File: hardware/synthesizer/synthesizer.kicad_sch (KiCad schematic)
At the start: 18 parts, among them J1 USB_C_Receptacle_PowerOnly_6P, J2 Conn_Coaxial, J3 Conn_Coaxial, U1 STM32H723VGTx

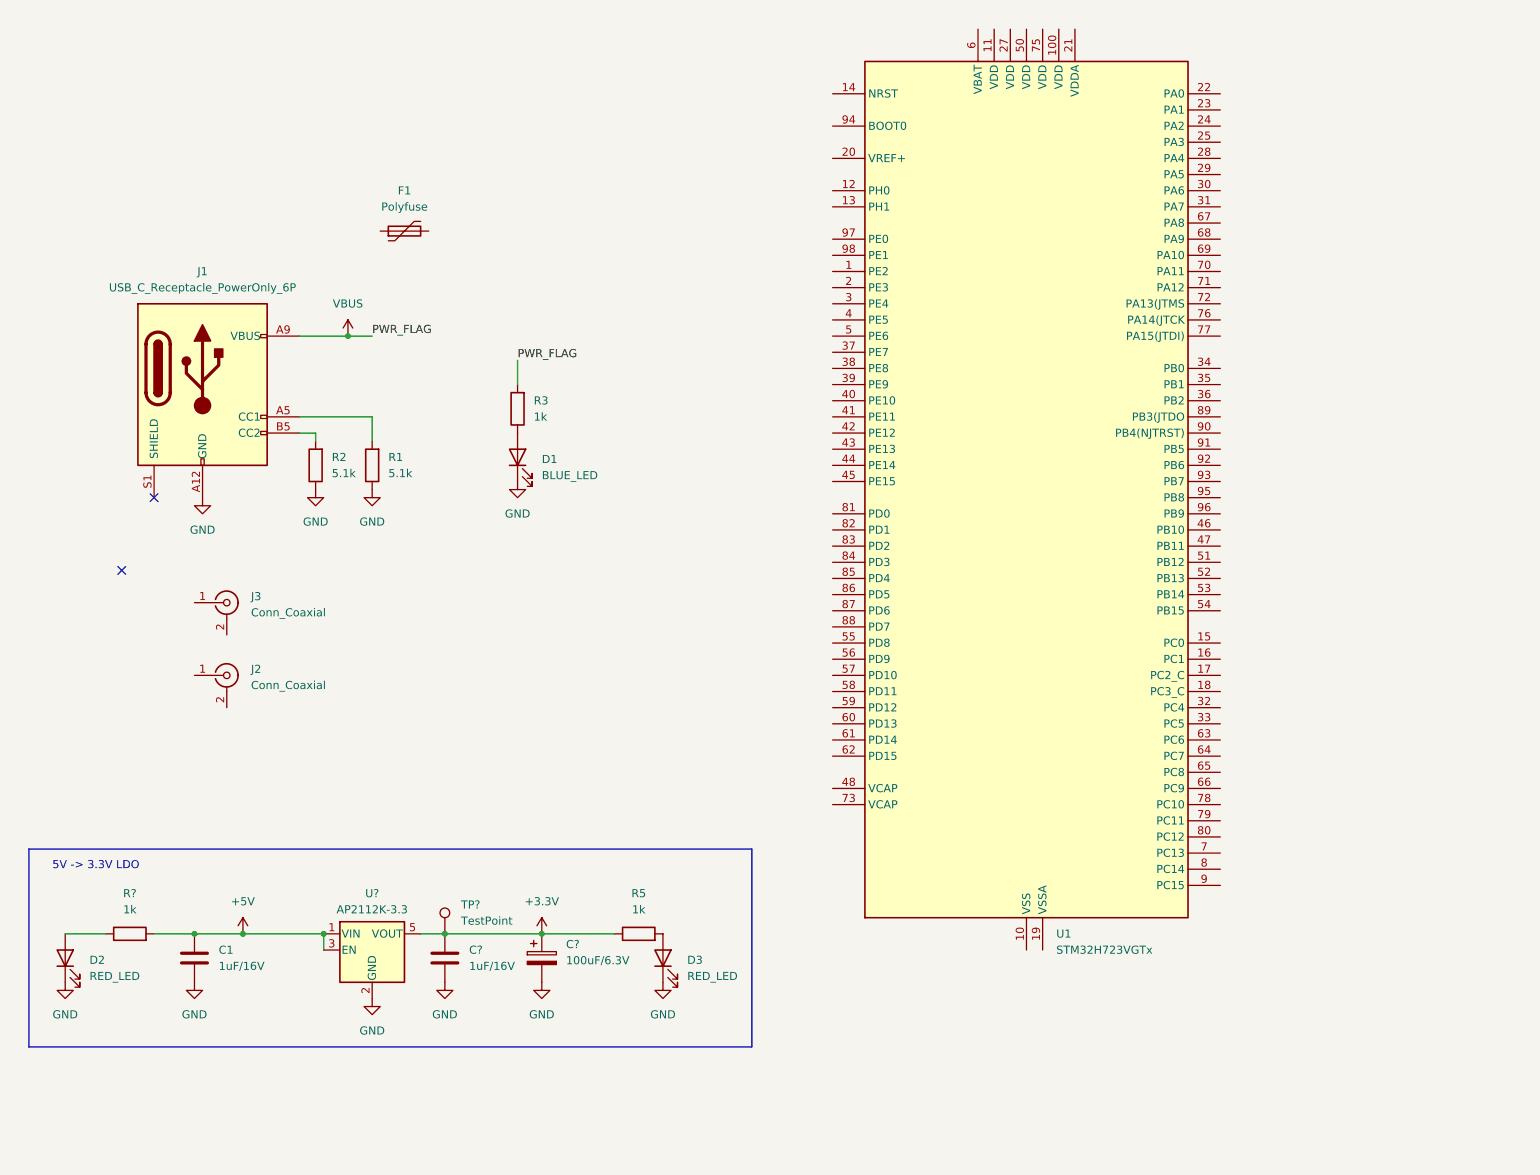
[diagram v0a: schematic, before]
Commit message: add jtag connector + continue cw8 report
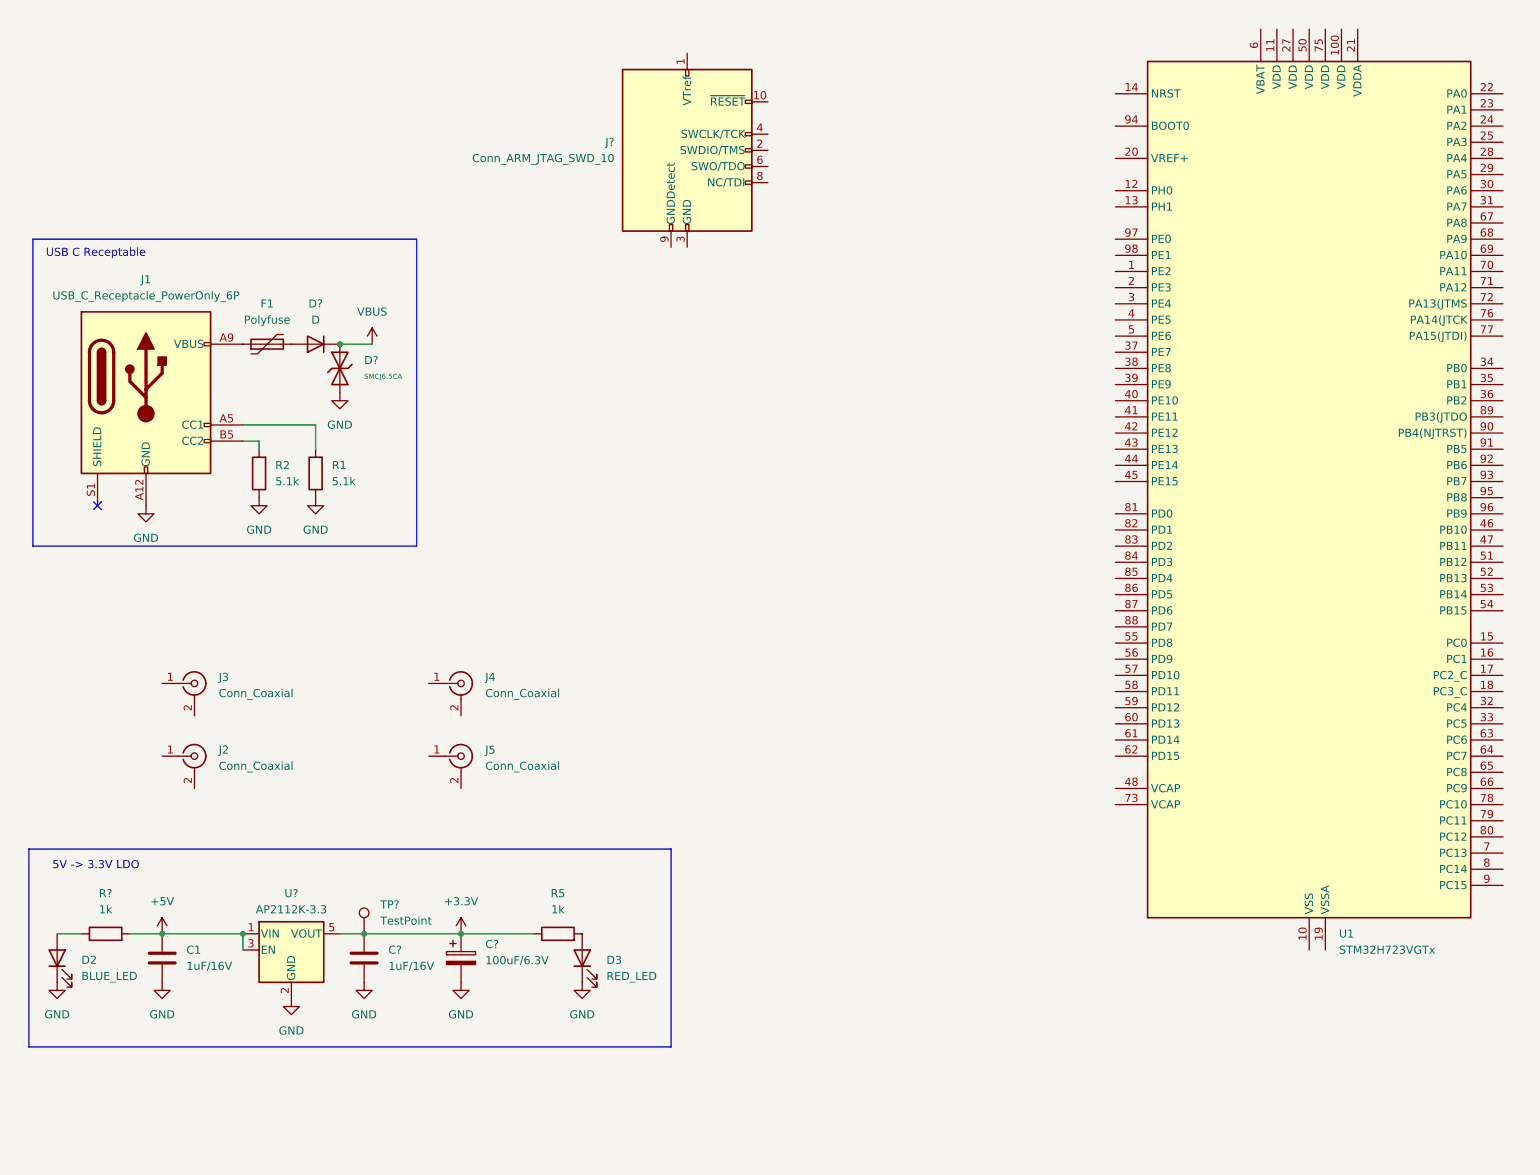
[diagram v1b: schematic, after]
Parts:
- removed D1: BLUE_LED, symbol Device:LED
- removed R3: 1k, symbol Device:R
- added D?: D, symbol Device:D
- added D?: SMCJ6.5CA, PCM_JLCPCB:D_SMC, symbol PCM_JLCPCB-Diodes:TVS-Bi,SMCJ6.5CA,(3)
- added J4, J5: Conn_Coaxial, Connector_Coaxial:SMA_BAT_Wireless_BWSMA-KWE-Z001, symbol Connector:Conn_Coaxial
- added J?: Conn_ARM_JTAG_SWD_10, Connector_PinHeader_1.27mm:PinHeader_2x05_P1.27mm_Vertical, symbol Connector:Conn_ARM_JTAG_SWD_10
- D2: value RED_LED -> BLUE_LED
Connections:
- net GND: now also D?.1
- net VBUS: now also D?.1 (K), D?.2; no longer J1.A9 (VBUS), J1.B9 (VBUS)
- net at F1.1: now also J1.A9 (VBUS), J1.B9 (VBUS)
- net at F1.2: now also D?.2 (A)
- new net: J?.3 (GND), J?.5 (GND)
- no-connect marks 2 -> 1
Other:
- note added: "USB C Receptable"
- moved on the sheet: C1, C?, D2, D3, F1, J1, J2, J3, R1, R2, R5, R?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

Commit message: add ethernet to synthesizer
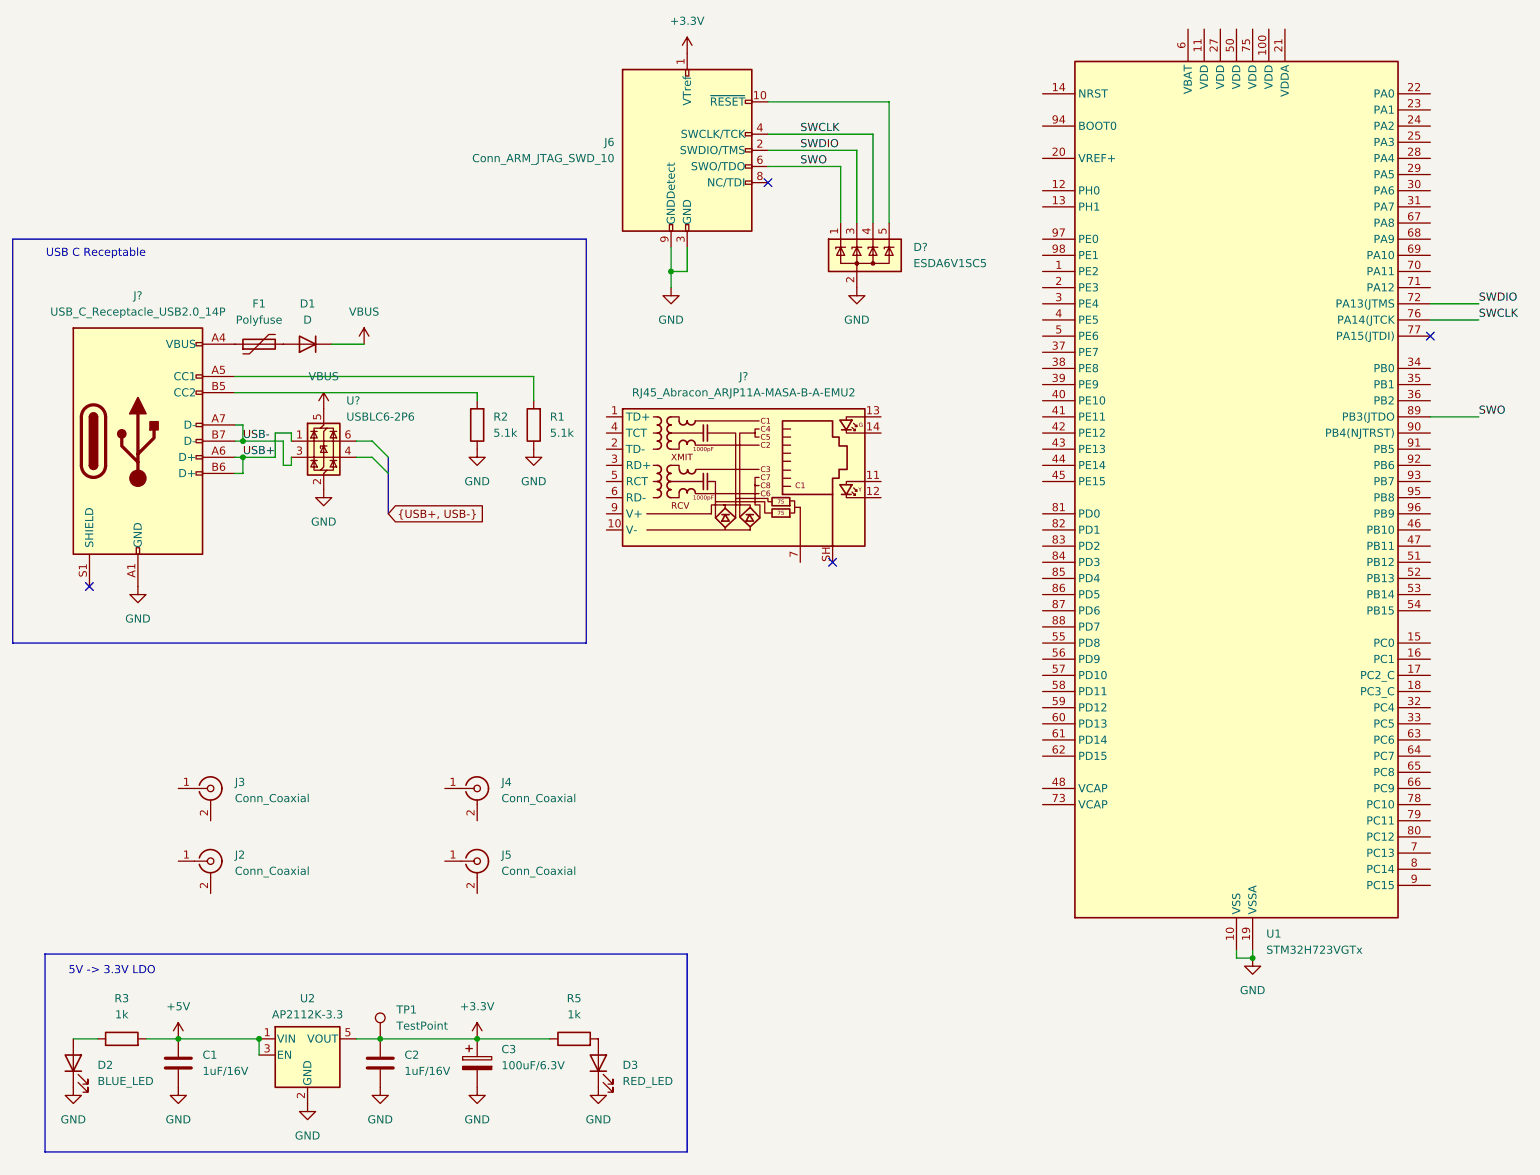
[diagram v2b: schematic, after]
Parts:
- removed D?: SMCJ6.5CA, PCM_JLCPCB:D_SMC, symbol PCM_JLCPCB-Diodes:TVS-Bi,SMCJ6.5CA,(3)
- removed J1: USB_C_Receptacle_PowerOnly_6P, Connector_USB:USB_C_Receptacle_GCT_USB4125-xx-x_6P_TopMnt_Horizontal, symbol Connector:USB_C_Receptacle_PowerOnly_6P
- added D?: ESDA6V1SC5, Package_TO_SOT_SMD:SOT-23-5, symbol Power_Protection:ESDA6V1SC5
- added J?: RJ45_Abracon_ARJP11A-MASA-B-A-EMU2, Connector_RJ:RJ45_Abracon_ARJP11A-MA_Horizontal, symbol Connector:RJ45_Abracon_ARJP11A-MASA-B-A-EMU2
- added J?: USB_C_Receptacle_USB2.0_14P, symbol Connector:USB_C_Receptacle_USB2.0_14P
- added U?: USBLC6-2P6, Package_TO_SOT_SMD:SOT-666, symbol Power_Protection:USBLC6-2P6
- D1: renamed from D?; footprint (none) -> Diode_SMD:D_0201_0603Metric
- F1: footprint (none) -> Fuse:Fuse_Bourns_MF-RG300
- gave numbers to parts that had none: 6
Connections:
- net +3.3V: now also J6.1 (VTref)
- net GND: now also J6.3 (GND), J6.5 (GND), J6.9 (GNDDetect), U1.10 (VSS), U1.19 (VSSA), U1.26 (VSS), U1.49 (VSS), U1.74 (VSS), U1.99 (VSS), D?.2 (A), J?.A1 (GND), J?.A12 (GND), J?.B1 (GND), J?.B12 (GND), U?.2 (GND)
- net VBUS: now also U?.5 (VBUS)
- net at J6.10 (~{RESET}): now also D?.5 (K)
- net SWDIO: now reaches J6.2 (SWDIO/TMS)
- net SWDIO: now also U1.72 (PA13(JTMS), D?.3 (K)
- net SWCLK: now reaches J6.4 (SWCLK/TCK)
- net SWCLK: now also U1.76 (PA14(JTCK), D?.4 (K)
- net SWO: now reaches J6.6 (SWO/TDO)
- net SWO: now also U1.89 (PB3(JTDO), D?.1 (K)
- net at R1.2: now also J?.A5 (CC1)
- net at F1.1: now also J?.A4 (VBUS), J?.A9 (VBUS), J?.B4 (VBUS), J?.B9 (VBUS)
- net at R2.2: now also J?.B5 (CC2)
- new net USB+: J?.A6 (D+), J?.B6 (D+), U?.1 (I/O1)
- new net USB-: J?.A7 (D-), J?.B7 (D-), U?.3 (I/O2)
- no-connect marks 1 -> 4
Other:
- moved on the sheet: C1, C2, C3, D1, D2, D3, F1, J2, J3, J4, J5, R1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

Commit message: improve report a bit
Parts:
- gave numbers to parts that had none: 4
